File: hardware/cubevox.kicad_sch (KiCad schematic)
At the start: 143 parts, among them J101 J_IN NCJ6FA-H, J106 DC 9V, J108 OUT 6.35mm, J117 OLED SH1106, K101 G6K-2F-Y DC5, SW104 EC11N1525404, SW105 EC11N1520401, SW106 EC11N1520401, SW107 ST-0-102 bat toggle, SW108 ST-0-102 bat toggle, SW109 ST-0-102 bat toggle, SW110 ST-0-102 bat toggle, SW111 ST-0-102 bat toggle, SW112 ST-0-102 bat toggle, SW113 ST-0-102 bat toggle, SW114 ST-0-102 bat toggle, SW115 ST-0-102 bat toggle, U101 CD74HC4067, U103 AP63205WU-7, U104 OPA1678IDR, U105 OPA1678IDR, U106 OPA1678IDR

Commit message: feat(hardware): refs RVGAIN/ENC101-103/SWBYPASS/SWBOOT/SWRESET, silk pass, control rows at 22.25 mm
Owner 2026-10-02: control rows y 165 (RV101-RV109) and y 130 (RV110-RV114,
RVGAIN, ENC101-103), 5 mm side padding, equal pitch. foreman silk applied;
one 1.0 mm designator on silk per pot/encoder/switch/jack, LCSC/MPN text
hidden. ERC 0, netlist parity 0/0/0.
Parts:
- removed RV115: 10k GAIN, cubevox:RES-ADJ-TH_RK09D1130C3C, symbol cubevox:RK09D1130C1B
- removed SW104: EC11N1525404, cubevox:SW-TH_EC11NXXXX, symbol cubevox:EC11N1525404
- removed SW105, SW106: EC11N1520401, cubevox:SW-TH_EC11NXXXX, symbol cubevox:EC11N1520401
- removed SW115: ST-0-102 bat toggle, cubevox:SW-TH_3P-L8.3-W5.2-P2.54_ST-0-102-A01-T000, symbol cubevox:ST-0-102-A01-T000-LF+PJ
- added ENC101: EC11N1525404, cubevox:SW-TH_EC11NXXXX, symbol cubevox:EC11N1525404
- added ENC102, ENC103: EC11N1520401, cubevox:SW-TH_EC11NXXXX, symbol cubevox:EC11N1520401
- added RVGAIN: 10k GAIN, cubevox:RES-ADJ-TH_RK09D1130C3C, symbol cubevox:RK09D1130C1B
- added SWBYPASS: ST-0-102 bat toggle, cubevox:SW-TH_3P-L8.3-W5.2-P2.54_ST-0-102-A01-T000, symbol cubevox:ST-0-102-A01-T000-LF+PJ
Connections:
- net 5V: now also SWBYPASS.1 (T1)
- net ENC_KEY_A: now also ENC102.A
- net ENC_KEY_B: now also ENC102.B
- net ENC_MENU_A: now also ENC101.A
- net ENC_MENU_B: now also ENC101.B
- net ENC_MENU_SW: now also ENC101.D
- net ENC_SEMI_A: now also ENC103.A
- net ENC_SEMI_B: now also ENC103.B
- net G2_FB: now also RVGAIN.2, RVGAIN.3
- net GND: now also ENC101.C, ENC101.E, ENC101.EH, ENC102.C, ENC102.EH, ENC103.C, ENC103.EH
- net PRE_OUT: now also RVGAIN.1
- net SW_BYPASS: now also SWBYPASS.2 (COM)
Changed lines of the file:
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@@
 		(on_board yes)
 		(dnp no)
-		(property "Reference" "RV115"
+		(property "Reference" "RVGAIN"
 			(at 645.16 326.39 0)
 			(effects
@@
 			(project "cubevox"
 				(path "/99ad1494-2bf8-5051-8886-2c8b83c86254"
-					(reference "RV115")
+					(reference "RVGAIN")
 					(unit 1)
 				)
@@
 		(on_board yes)
 		(dnp no)
-		(property "Reference" "SW115"
+		(property "Reference" "SWBYPASS"
 			(at 1018.54 162.56 0)
 			(effects
@@
 			(project "cubevox"
 				(path "/99ad1494-2bf8-5051-8886-2c8b83c86254"
-					(reference "SW115")
+					(reference "SWBYPASS")
 					(unit 1)
 				)
@@
 		(on_board yes)
 		(dnp no)
-		(property "Reference" "SW104"
+		(property "Reference" "ENC101"
 			(at 154.94 595.63 0)
 			(effects
@@
 			(project "cubevox"
 				(path "/99ad1494-2bf8-5051-8886-2c8b83c86254"
-					(reference "SW104")
+					(reference "ENC101")
 					(unit 1)
 				)
@@
 		(on_board yes)
 		(dnp no)
-		(property "Reference" "SW105"
+		(property "Reference" "ENC102"
 			(at 332.74 595.63 0)
 			(effects
@@
 			(project "cubevox"
 				(path "/99ad1494-2bf8-5051-8886-2c8b83c86254"
-					(reference "SW105")
+					(reference "ENC102")
 					(unit 1)
 				)
@@
 		(on_board yes)
 		(dnp no)
-		(property "Reference" "SW106"
+		(property "Reference" "ENC103"
 			(at 510.54 595.63 0)
 			(effects
@@
 			(project "cubevox"
 				(path "/99ad1494-2bf8-5051-8886-2c8b83c86254"
-					(reference "SW106")
+					(reference "ENC103")
 					(unit 1)
 				)

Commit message: feat(hardware): SH1106 1.3in OLED module footprint + model; owner's panel layout; refs end in 1
Footprint OLED-1.3-SH1106-I2C-4P from the vendor drawings (35.4x33.5,
holes 30.4x28.5, 4-pin header GND/VCC/SCL/SDA, active area on User.1),
STEP on 8 mm standoffs. J117 pins now GND, 3V3, SCL, SDA. Panel: bypass
and gain under the jacks, OLED + menu encoder centred, eight stage
columns with KEY and SEMITONES in columns 1-2. RVGAIN1 / SWBYPASS1 /
SWBOOT1 / SWRESET1 clear KiCad's annotation warning. ERC 0, parity 0/0/0.
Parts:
- removed RVGAIN: 10k GAIN, cubevox:RES-ADJ-TH_RK09D1130C3C, symbol cubevox:RK09D1130C1B
- removed SWBYPASS: ST-0-102 bat toggle, cubevox:SW-TH_3P-L8.3-W5.2-P2.54_ST-0-102-A01-T000, symbol cubevox:ST-0-102-A01-T000-LF+PJ
- added RVGAIN1: 10k GAIN, cubevox:RES-ADJ-TH_RK09D1130C3C, symbol cubevox:RK09D1130C1B
- added SWBYPASS1: ST-0-102 bat toggle, cubevox:SW-TH_3P-L8.3-W5.2-P2.54_ST-0-102-A01-T000, symbol cubevox:ST-0-102-A01-T000-LF+PJ
- J117: footprint cubevox:HDR-TH_4P-P2.54-V-M -> cubevox:OLED-1.3-SH1106-I2C-4P; symbol cubevox:PZ254V-11-04P_C2691448 -> cubevox:OLED-1.3-SH1106-I2C-4P; LCSC C2691448 -> owner-supplied module, hand-plugged; MPN PZ254V-11-04P -> SH1106 1.3in I2C 128x64
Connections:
- net 3V3: now also J117.2 (VCC); no longer J117.1
- net 5V: now also SWBYPASS1.1 (T1)
- net G2_FB: now also RVGAIN1.2, RVGAIN1.3
- net GND: now also J117.1 (GND); no longer J117.2
- net PRE_OUT: now also RVGAIN1.1
- net SW_BYPASS: now also SWBYPASS1.2 (COM)
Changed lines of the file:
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@@
 		(on_board yes)
 		(dnp no)
-		(property "Reference" "RVGAIN"
+		(property "Reference" "RVGAIN1"
 			(at 645.16 326.39 0)
 			(effects
@@
 			(project "cubevox"
 				(path "/99ad1494-2bf8-5051-8886-2c8b83c86254"
-					(reference "RVGAIN")
+					(reference "RVGAIN1")
 					(unit 1)
 				)
@@
 		(on_board yes)
 		(dnp no)
-		(property "Reference" "SWBYPASS"
+		(property "Reference" "SWBYPASS1"
 			(at 1018.54 162.56 0)
 			(effects
@@
 			(project "cubevox"
 				(path "/99ad1494-2bf8-5051-8886-2c8b83c86254"
-					(reference "SWBYPASS")
+					(reference "SWBYPASS1")
 					(unit 1)
 				)
@@
 	)
 	(symbol
-		(lib_id "cubevox:PZ254V-11-04P_C2691448")
+		(lib_id "cubevox:OLED-1.3-SH1106-I2C-4P")
 		(at 797.56 596.9 0)
 		(unit 1)
@@
 			)
 		)
-		(property "Footprint" "cubevox:HDR-TH_4P-P2.54-V-M"
+		(property "Footprint" "cubevox:OLED-1.3-SH1106-I2C-4P"
 			(at 797.56 596.9 0)
 			(hide yes)
@@
 			)
 		)
-		(property "LCSC" "C2691448"
+		(property "LCSC" "owner-supplied module, hand-plugged"
 			(at 797.56 596.9 0)
 			(hide yes)
@@
 			)
 		)
-		(property "MPN" "PZ254V-11-04P"
+		(property "MPN" "SH1106 1.3in I2C 128x64"
 			(at 797.56 596.9 0)
 			(hide yes)
@@
 		)
 	)
-	(label "3V3"
+	(label "GND"
 		(at 791.21 593.09 180)
 		(fields_autoplaced yes)
@@
 		)
 	)
-	(label "GND"
+	(label "3V3"
 		(at 791.21 595.63 180)
 		(fields_autoplaced yes)

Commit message: fix(hardware): toggles SW101-SW108 left to right; groups removed, nothing locked
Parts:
- removed SW109, SW110, SW111, SW112, SW113, SW114: ST-0-102 bat toggle, cubevox:SW-TH_3P-L8.3-W5.2-P2.54_ST-0-102-A01-T000, symbol cubevox:ST-0-102-A01-T000-LF+PJ
- added SW101, SW102, SW103, SW104, SW105, SW106: ST-0-102 bat toggle, cubevox:SW-TH_3P-L8.3-W5.2-P2.54_ST-0-102-A01-T000, symbol cubevox:ST-0-102-A01-T000-LF+PJ
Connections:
- net GND: now also SW101.1 (T1), SW102.1 (T1), SW103.1 (T1), SW104.1 (T1), SW105.1 (T1), SW106.1 (T1)
- net TOGGLE1: now also SW101.2 (COM); no longer SW107.2 (COM)
- net TOGGLE2: now also SW102.2 (COM); no longer SW108.2 (COM)
- net TOGGLE3: now also SW103.2 (COM)
- net TOGGLE4: now also SW104.2 (COM)
- net TOGGLE5: now also SW105.2 (COM)
- net TOGGLE6: now also SW106.2 (COM)
- net TOGGLE7: now also SW107.2 (COM)
- net TOGGLE8: now also SW108.2 (COM)
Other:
- moved on the sheet: SW107, SW108
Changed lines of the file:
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@@
 		(on_board yes)
 		(dnp no)
-		(property "Reference" "SW107"
+		(property "Reference" "SW101"
 			(at 233.68 708.66 0)
 			(effects
@@
 			(project "cubevox"
 				(path "/99ad1494-2bf8-5051-8886-2c8b83c86254"
-					(reference "SW107")
+					(reference "SW101")
 					(unit 1)
 				)
@@
 		(on_board yes)
 		(dnp no)
-		(property "Reference" "SW108"
+		(property "Reference" "SW102"
 			(at 373.38 708.66 0)
 			(effects
@@
 			(project "cubevox"
 				(path "/99ad1494-2bf8-5051-8886-2c8b83c86254"
-					(reference "SW108")
+					(reference "SW102")
 					(unit 1)
 				)
@@
 		(on_board yes)
 		(dnp no)
-		(property "Reference" "SW109"
+		(property "Reference" "SW103"
 			(at 513.08 708.66 0)
 			(effects
@@
 			(project "cubevox"
 				(path "/99ad1494-2bf8-5051-8886-2c8b83c86254"
-					(reference "SW109")
+					(reference "SW103")
 					(unit 1)
 				)
@@
 		(on_board yes)
 		(dnp no)
-		(property "Reference" "SW110"
+		(property "Reference" "SW104"
 			(at 652.78 708.66 0)
 			(effects
@@
 			(project "cubevox"
 				(path "/99ad1494-2bf8-5051-8886-2c8b83c86254"
-					(reference "SW110")
+					(reference "SW104")
 					(unit 1)
 				)
@@
 		(on_board yes)
 		(dnp no)
-		(property "Reference" "SW111"
+		(property "Reference" "SW105"
 			(at 233.68 772.16 0)
 			(effects
@@
 			(project "cubevox"
 				(path "/99ad1494-2bf8-5051-8886-2c8b83c86254"
-					(reference "SW111")
+					(reference "SW105")
 					(unit 1)
 				)
@@
 		(on_board yes)
 		(dnp no)
-		(property "Reference" "SW112"
+		(property "Reference" "SW106"
 			(at 373.38 772.16 0)
 			(effects
@@
 			(project "cubevox"
 				(path "/99ad1494-2bf8-5051-8886-2c8b83c86254"
-					(reference "SW112")
+					(reference "SW106")
 					(unit 1)
 				)
@@
 		(on_board yes)
 		(dnp no)
-		(property "Reference" "SW113"
+		(property "Reference" "SW107"
 			(at 513.08 772.16 0)
 			(effects
@@
 			(project "cubevox"
 				(path "/99ad1494-2bf8-5051-8886-2c8b83c86254"
-					(reference "SW113")
+					(reference "SW107")
 					(unit 1)
 				)
@@
 		(on_board yes)
 		(dnp no)
-		(property "Reference" "SW114"
+		(property "Reference" "SW108"
 			(at 652.78 772.16 0)
 			(effects
@@
 			(project "cubevox"
 				(path "/99ad1494-2bf8-5051-8886-2c8b83c86254"
-					(reference "SW114")
+					(reference "SW108")
 					(unit 1)
 				)

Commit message: feat(hardware): revision 2 analog chain in schematic, board and parts
Implements the accepted audit findings: OPA2197 preamp with AC-coupled
gain legs (DC gain 1), 0.1 % difference amp, isolated VREF follower
(22 R + 10 uF), pot-as-feedback stage 2 over 200 R + 100 uF, DAC and
output coupling as electrolytics, both NCJ6FA-H T pads tied (no sense
GPIO), ADC SCKI from SAI1_MCLK_A on PE2 with QSPI moved to bank 2.
ERC 0, netlist parity 0/0/0, owner-placed panel parts unmoved. Adds
the audit, its response, and the evidence capture.
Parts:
- removed C122, C126, C131, C133, C140: 100nF, cubevox:C0603, symbol Device:C
- removed R107: 10k, cubevox:R0603, symbol Device:R
- removed R115: 100R, cubevox:R0603, symbol Device:R
- added C158: 22uF 16V, cubevox:CAP-SMD_BD4.0-L4.3-W4.3-LS5.3-FD, symbol cubevox:RVT1C220M0405
- added C159: 100uF 10V, cubevox:CAP-SMD_BD5.0-L5.3-W5.3-LS6.3-FD, symbol cubevox:VT1A101M0505
- added C160: 10uF 25V, cubevox:CAP-SMD_BD4.0-L4.3-W4.3-FD, symbol cubevox:RVT1E100M0405-C72484
- added C161: 2.2nF, cubevox:C0603, symbol Device:C
- added R144, R145: 100k, cubevox:R0603, symbol Device:R
- added R146: 22R, cubevox:R0603, symbol Device:R
- added R147: 470R, cubevox:R0603, symbol Device:R
- C120, C121, C124, C125, C139, C141: value 10uF -> 10uF 25V; footprint cubevox:C1206 -> cubevox:CAP-SMD_BD4.0-L4.3-W4.3-FD; symbol Device:C -> cubevox:RVT1E100M0405-C72484; LCSC C14860 -> C72484; MPN (none) -> RVT1E100M0405
- R108, R110: value 4.7k -> 9.53k; LCSC C23162 -> C23127
- R111, R112, R113, R114: value 10k -> 10k 0.1%; LCSC C25804 -> C309083; MPN (none) -> ARG03BTC1002
- R116: value 100R -> 200R; LCSC C22775 -> C8218
- U104, U105, U106: value OPA1678IDR -> OPA2197IDR; footprint cubevox:SOIC-8_L5.0-W4.0-P1.27-LS6.0-BL -> cubevox:SOIC-8_L4.9-W3.9-P1.27-LS6.0-BL; symbol cubevox:OPA1678IDR -> cubevox:OPA2197IDR; LCSC C192421 -> C139363; MPN OPA1678IDR -> OPA2197IDR
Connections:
- net G2_FB is gone; now on net G2_INV: RVGAIN1.2, RVGAIN1.3
- net JACK_TRS_N is gone; now on net TRS_T: J101.7 (T_SW)
- net A1_FB: now also C158.1; no longer R109.1
- net DAC_AC: now also C139.1; no longer C139.2
- net DAC_OUTL: now also R147.1; no longer C139.1
- net GND: now also C159.2, C160.2, C161.2, R144.2, R145.2
- net IN_N: now also C124.1; no longer C124.2
- net IN_P: now also C120.1; no longer C120.2
- net LINE_N: now also C125.1; no longer C125.2
- net LINE_P: now also C121.1; no longer C121.2
- net MIC_N: now also C124.2, R145.1; no longer C124.1
- net MIC_P: now also C120.2, R144.1; no longer C120.1
- net TRS_R: now also C125.2; no longer C125.1
- net TRS_T: now also C121.2; no longer C121.1
- net VREF: now also C160.1, R146.2; no longer R116.2, U106.1 (OUTA), U106.2 (INA-)
- new net DAC_LP: C139.2, C161.1, R147.2
- new net G2_RG: C159.1, R116.2
- new net RG_MID: C158.2, R109.1
- new net VREF_BUF: R146.1, U106.1 (OUT/A), U106.2 (-IN/A)
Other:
- sheet h7core_block ports: added none; removed JACK_TRS_N
- note added: "470R / 2.2nF filter, 10uF, DAC_ATT = 0.6 x DAC about VREF"
- note added: "Both T holes are the tip (Neutrik: one tip circuit, no switch). No plug detection"
- note added: "Input Gain pot is the A4 feedback resistor, wiper tied to end 3. G = 1 + Rpot/200"
- note added: "RG = R109 1k + C158 22uF in series, DC gain 1. Gain 1 + 2 x 9.53k / 1k = 20.1"
- note added: "Stage 1 26.0 dB, stage 2 0-34.2 dB, chain 26-60 dB XLR / 6.6-40.8 dB TRS; DC gain 1 (AC-coupled legs)"
- note added: "Stage 1 INA 26 dB (U104, U105A). Stage 2 0-34.2 dB on Input Gain pot (U105B)"
- note added: "U106B buffers to the jack"
- note added: "VREF: 5VA divided 10k/10k, 10 uF, follower U106A, 22R into VREF with 10 uF. U106B drives block 6"
- note added: "XLR leg 47R, BAT54S clamp, 100pF, 100k to GND, 10uF + IN_x. TRS leg 10uF + LINE_x, 10k pad. 1.2k bias to VREF"
- note removed: "DAC_ATT = 0.6 x DAC about VREF. U106B buffers to the jack"
- note removed: "Input Gain pot in the A4 feedback leg, wiper tied to end 3"
- note removed: "JACK_TRS_N low when a 1/4 in plug is in"
- note removed: "Stage 1 INA 20 dB (U104, U105A). Stage 2 0-40 dB on Input Gain pot (U105B)"
- note removed: "VREF: 5VA divided 10k/10k, 10 uF, buffered by U106A. U106B drives block 6"
- note removed: "XLR leg 47R, BAT54S clamp, 100pF, 10uF. TRS leg 10uF, 10k pad. 1.2k bias to VREF"
- moved on the sheet: R116

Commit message: feat(hardware): revision 3 analog chain, 9 V only, no external flash
Removes the QSPI flash, the TPS2116 USB power mux and the duplicate M2
OLED holes. Settings live in internal flash bank 2; USB is data only.
Codex round 2 (hardware/audit) accepted: stage 1 20 dB, TRS pad -25.7 dB,
47 uF mic coupling, bipolar C158, R116 330 R, relay pole B as the
FX_ON_SENSE dry contact, VBUS divider 33k/82k on PA9, output mute relay
K102 on PD12 with 5VA sense on PC4. ERC 0, netlist parity 0/0/0, panel
parts unmoved.
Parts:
- removed H105, H106, H107, H108: M2 OLED, MountingHole:MountingHole_2.2mm_M2, symbol Mechanical:MountingHole
- removed R121: 18k, cubevox:R0603, symbol Device:R
- added C162, C163: 100nF, cubevox:C0603, symbol Device:C
- added D109: 1N4148W, cubevox:SOD-123F_L2.7-W1.6-LS3.8-RD, symbol cubevox:1N4148W_C81598
- added K102: G6K-2F-Y DC5, cubevox:RELAY-SMD_G6K-2F-X-XX, symbol cubevox:G6K-2F-Y-DC5
- added Q101: MMBT3904, cubevox:SOT-23-3_L2.9-W1.3-P1.90-LS2.4-BR, symbol cubevox:MMBT3904-C20526
- added R148, R149, R153: 100k, cubevox:R0603, symbol Device:R
- added R150: 1k, cubevox:R0603, symbol Device:R
- added R151, R152: 10k, cubevox:R0603, symbol Device:R
- C120, C124: value 10uF 25V -> 47uF 25V; footprint cubevox:CAP-SMD_BD4.0-L4.3-W4.3-FD -> cubevox:CAP-SMD_BD6.3-L6.6-W6.6-LS7.6-FD; symbol cubevox:RVT1E100M0405-C72484 -> cubevox:RVT1E470M0605; LCSC C72484 -> C72521; MPN RVT1E100M0405 -> RVT1E470M0605
- C158: value 22uF 16V -> 22uF 25V NP; footprint cubevox:CAP-SMD_BD4.0-L4.3-W4.3-LS5.3-FD -> cubevox:CAP-SMD_BD6.3-L6.6-W6.6-FD; symbol cubevox:RVT1C220M0405 -> Device:C; LCSC C72502 -> C413679; MPN RVT1C220M0405 -> EEEHP1E220P
- R102, R105: value 10k -> 22k; LCSC C25804 -> C31850
- R108, R110: value 9.53k -> 4.53k; LCSC C23127 -> C25971
- R116: value 200R -> 330R; LCSC C8218 -> C23138
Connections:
- net 5V_PRODUCT is gone; now on net 5V: C114.1, C115.1, L101.2, U103.1 (FB)
- net 3V3: now also R120.1
- net 5V: now also D109.1 (K), K102.1
- net 5VA: now also R151.1
- net BUF_IN: no longer K101.6
- net DAC_ATT: no longer K101.5
- net FX_ON_SENSE: now also K101.5, C162.1
- net GND: now also K101.6, C162.2, C163.2, K102.7, Q101.2 (E), R148.2, R149.2, R152.2, R153.2
- net OUT_TIP: now also K102.4, K102.6; no longer C141.2, R125.1
- net PRE_OUT: no longer K101.7
- net SW_BYPASS: no longer R120.1
- net TRS_R: now also R149.1
- net TRS_T: now also R148.1
- new net MUTE_BASE: Q101.1 (B), R150.2, R153.1
- new net MUTE_COIL: D109.2 (A), K102.8, Q101.3 (C)
- new net MUTE_N: R150.1
- new net OUT_AC: C141.2, K102.3, R125.1
- new net VA_SENSE: C163.1, R151.2, R152.1
- no-connect marks 52 -> 55
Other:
- sheet h7core_block ports: added MUTE_N, VA_SENSE; removed 5V_PRODUCT
- note added: "5VA SENSE"
- note added: "8. OUTPUT MUTE"
- note added: "Chain 20-50 dB XLR / -5.6 to +24.3 dB TRS; DC gain 1 (AC-coupled legs)"
- note added: "Input Gain pot is the A4 feedback resistor, wiper tied to end 3. G = 1 + Rpot/330"
- note added: "K102 closes OUT_AC to OUT_TIP when MUTE_N is high, else OUT_TIP is grounded"
- note added: "OUT_TIP via K102 (section 8)"
- note added: "Pole A COM BUF_IN, NC PRE_OUT, NO DAC_ATT. Pole B COM GND, NO FX_ON_SENSE (low = effect on). Coil on = effect on"
- note added: "RG = R109 1k + C158 22uF bipolar in series, DC gain 1. Gain 1 + 2 x 4.53k / 1k = 10.06"
- note added: "Stage 1 INA 20.05 dB (U104, U105A). Stage 2 0-29.9 dB on Input Gain pot (U105B)"
- note added: "XLR leg 47R, BAT54S clamp, 100pF, 100k to GND, 47uF + IN_x. TRS leg 10uF + LINE_x, 22k pad, 100k to GND. 1.2k bias to VREF"
- note removed: "COM BUF_IN, NC PRE_OUT, NO DAC_ATT. Coil on = effect on"
- note removed: "Input Gain pot is the A4 feedback resistor, wiper tied to end 3. G = 1 + Rpot/200"
- note removed: "RG = R109 1k + C158 22uF in series, DC gain 1. Gain 1 + 2 x 9.53k / 1k = 20.1"
- note removed: "Stage 1 26.0 dB, stage 2 0-34.2 dB, chain 26-60 dB XLR / 6.6-40.8 dB TRS; DC gain 1 (AC-coupled legs)"
- note removed: "Stage 1 INA 26 dB (U104, U105A). Stage 2 0-34.2 dB on Input Gain pot (U105B)"
- note removed: "XLR leg 47R, BAT54S clamp, 100pF, 100k to GND, 10uF + IN_x. TRS leg 10uF + LINE_x, 10k pad. 1.2k bias to VREF"

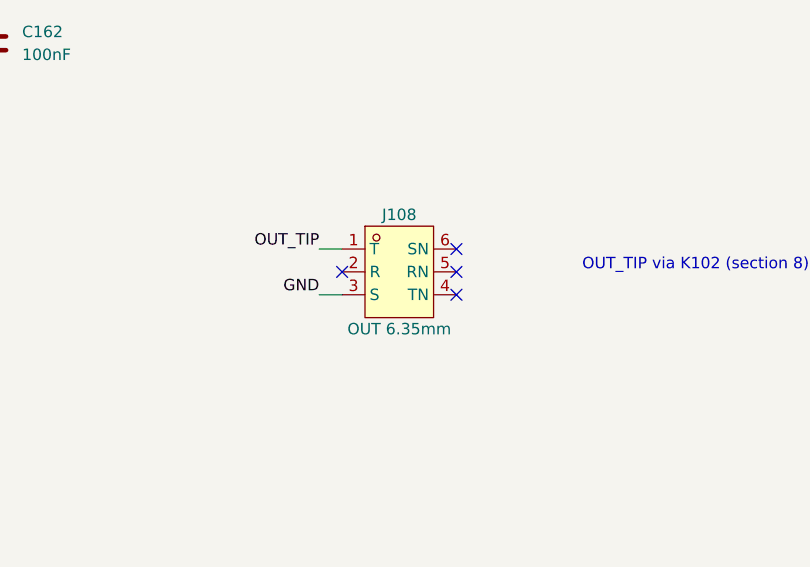
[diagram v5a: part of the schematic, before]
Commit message: feat(hardware): output jack J108 is HOOYA PJ-611E (C309282)
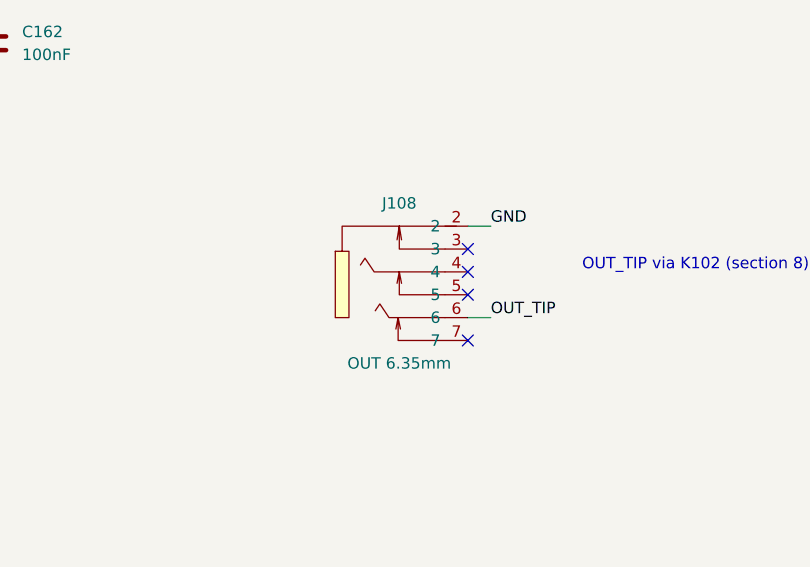
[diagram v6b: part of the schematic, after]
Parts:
- J108: footprint cubevox:AUDIO-TH_NMJ6HCD2 -> cubevox:AUDIO-TH_PJ-611E_1; symbol cubevox:NMJ6HCD2 -> cubevox:PJ-611E; LCSC C368502 -> C309282; MPN NMJ6HCD2 -> PJ-611E
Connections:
- net GND: now also J108.2; no longer J108.3 (S)
- net OUT_TIP: now also J108.6; no longer J108.1 (T)
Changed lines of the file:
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@@
 	)
 	(symbol
-		(lib_id "cubevox:NMJ6HCD2")
+		(lib_id "cubevox:PJ-611E")
 		(at 1092.2 254 0)
 		(unit 1)
@@
 		(dnp no)
 		(property "Reference" "J108"
-			(at 1092.2 247.65 0)
+			(at 1092.2 246.38 0)
 			(effects
 				(font
@@
 		)
 		(property "Value" "OUT 6.35mm"
-			(at 1092.2 260.35 0)
+			(at 1092.2 264.16 0)
 			(effects
 				(font
@@
 			)
 		)
-		(property "Footprint" "cubevox:AUDIO-TH_NMJ6HCD2"
+		(property "Footprint" "cubevox:AUDIO-TH_PJ-611E_1"
 			(at 1092.2 254 0)
 			(hide yes)
@@
 			)
 		)
-		(property "LCSC" "C368502"
+		(property "LCSC" "C309282"
 			(at 1092.2 254 0)
 			(hide yes)
@@
 			)
 		)
-		(property "MPN" "NMJ6HCD2"
+		(property "MPN" "PJ-611E"
 			(at 1092.2 254 0)
 			(hide yes)
@@
 				)
 			)
-		)
-		(pin "1"
 		)
 		(pin "2"
@@
 		)
 		(pin "6"
+		)
+		(pin "7"
 		)
 		(instances
@@
 	(wire
 		(pts
-			(xy 1085.85 251.46) (xy 1083.31 251.46)
+			(xy 1099.82 248.92) (xy 1102.36 248.92)
+		)
+		(stroke
+			(width 0)
+			(type default)
+		)
+	)
+	(label "GND"
+		(at 1102.36 248.92 0)
+		(fields_autoplaced yes)
+		(effects
+			(font
+				(size 1.27 1.27)
+			)
+			(justify left bottom)
+		)
+	)
+	(no_connect
+		(at 1099.82 251.46)
+	)
+	(no_connect
+		(at 1099.82 254)
+	)
+	(no_connect
+		(at 1099.82 256.54)
+	)
+	(wire
+		(pts
+			(xy 1099.82 259.08) (xy 1102.36 259.08)
 		)
 		(stroke
@@
 	)
 	(label "OUT_TIP"
-		(at 1083.31 251.46 180)
+		(at 1102.36 259.08 0)
 		(fields_autoplaced yes)
 		(effects
@@
 				(size 1.27 1.27)
 			)
-			(justify right bottom)
+			(justify left bottom)
 		)
 	)
 	(no_connect
-		(at 1085.85 254)
-	)
-	(wire
-		(pts
-			(xy 1085.85 256.54) (xy 1083.31 256.54)
-		)
-		(stroke
-			(width 0)
-			(type default)
-		)
-	)
-	(label "GND"
-		(at 1083.31 256.54 180)
-		(fields_autoplaced yes)
-		(effects
-			(font
-				(size 1.27 1.27)
-			)
-			(justify right bottom)
-		)
-	)
-	(no_connect
-		(at 1098.55 256.54)
-	)
-	(no_connect
-		(at 1098.55 254)
-	)
-	(no_connect
-		(at 1098.55 251.46)
+		(at 1099.82 261.62)
 	)
 	(symbol
